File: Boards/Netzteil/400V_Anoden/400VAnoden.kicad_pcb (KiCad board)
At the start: 2 copper layers, 160 x 100 mm, 52 parts, among them P1 Drossel, P2 320V_AC, P3 Stabi, P4 133V_AC, P5 Stabi, P6 Trafo, P7 Trafo, P8 Relay, Q1 2SC2979

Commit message: Work in progess - many LAyour changes
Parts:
- added J1: Chassis_GND, MountingHole:MountingHole_3.2mm_M3_Pad_Via, F.Cu at (111.8, 111.8)
- moved REF** 9.03 mm to (111.8, 121.3)
- moved C2 4.70 mm to (59.1, 48.8)
- moved C8 4.70 mm to (59.1, 69.5)
- moved D2 3.81 mm to (69.2, 54.0)
- moved D4 3.81 mm to (67.3, 71.9)
- moved R1 3.81 mm to (79.4, 62.2)
- moved C15 1.91 mm to (65.4, 113.0)
- moved C16 1.91 mm to (65.4, 94.6)
- moved D7 1.91 mm to (75.6, 107.7)
- moved D8 1.91 mm to (85.7, 100.1)
- moved C12 1.52 mm to (84.1, 94.6)
- moved D10 1.52 mm to (56.1, 100.1)
- moved D9 1.52 mm to (66.3, 107.7)
- moved R8 1.52 mm to (70.9, 89.9)
- moved C11 1.52 mm to (84.0, 113.0)
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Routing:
- net Net-(C3-Pad1): track 99.6 -> 85.0 mm
- net Net-(C1-Pad1): track 49.3 -> 44.8 mm
- net Net-(C5-Pad1): track 227.6 -> 230.8 mm
- net Net-(C15-Pad2): track 26.4 -> 28.2 mm
- net Net-(C11-Pad1): track 31.6 -> 30.0 mm
- net /-180V_DC: track 167.4 -> 165.8 mm
- net Net-(C7-Pad2): track 74.1 -> 72.8 mm
- net Net-(D11-Pad2): track 26.6 -> 27.5 mm
- net Net-(D11-Pad1): track 31.0 -> 30.3 mm
- net GND: vias 46 -> 44
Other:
- rule pad_to_mask_clearance: 0.2 -> 0
- board text added: "Chassis GND"

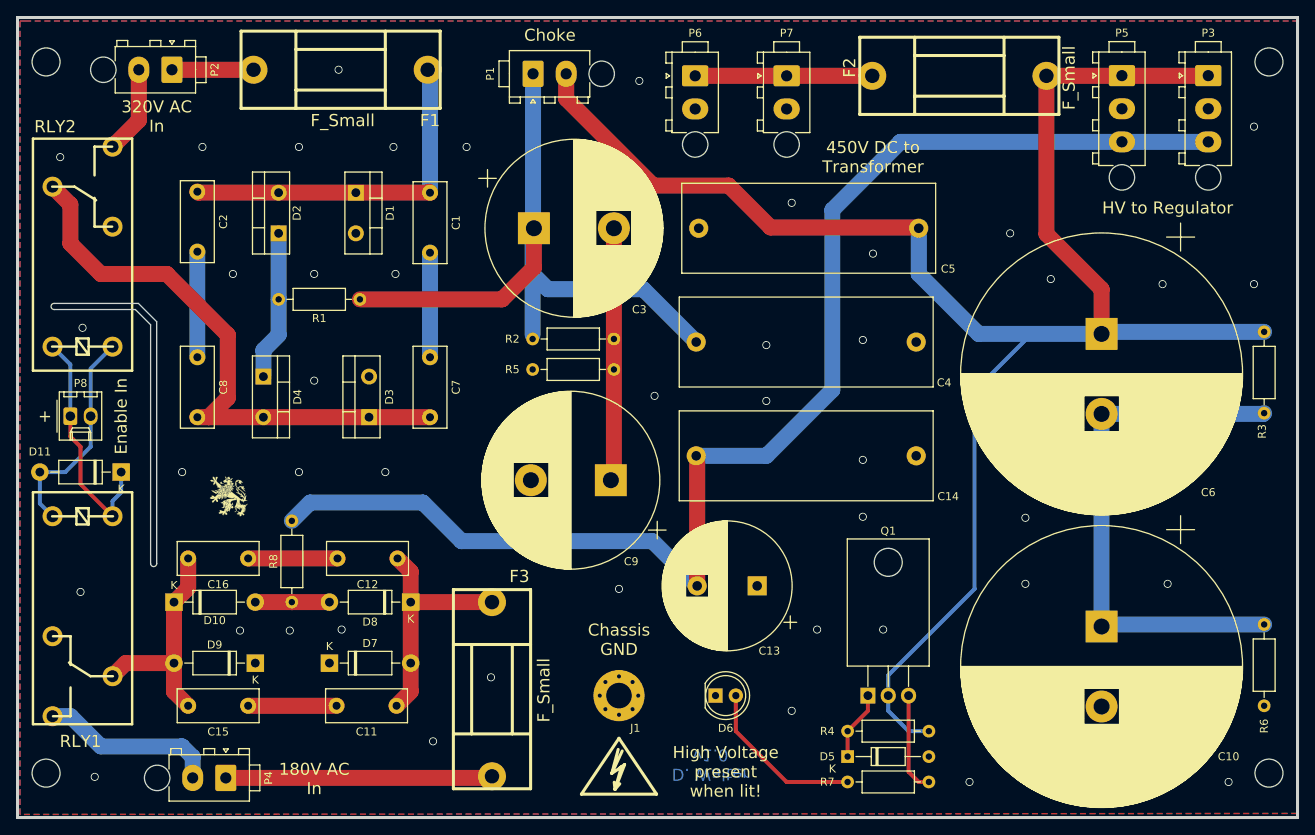
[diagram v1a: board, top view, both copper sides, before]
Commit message: 6.3V, 400V und 400V Regler Boards bestellt
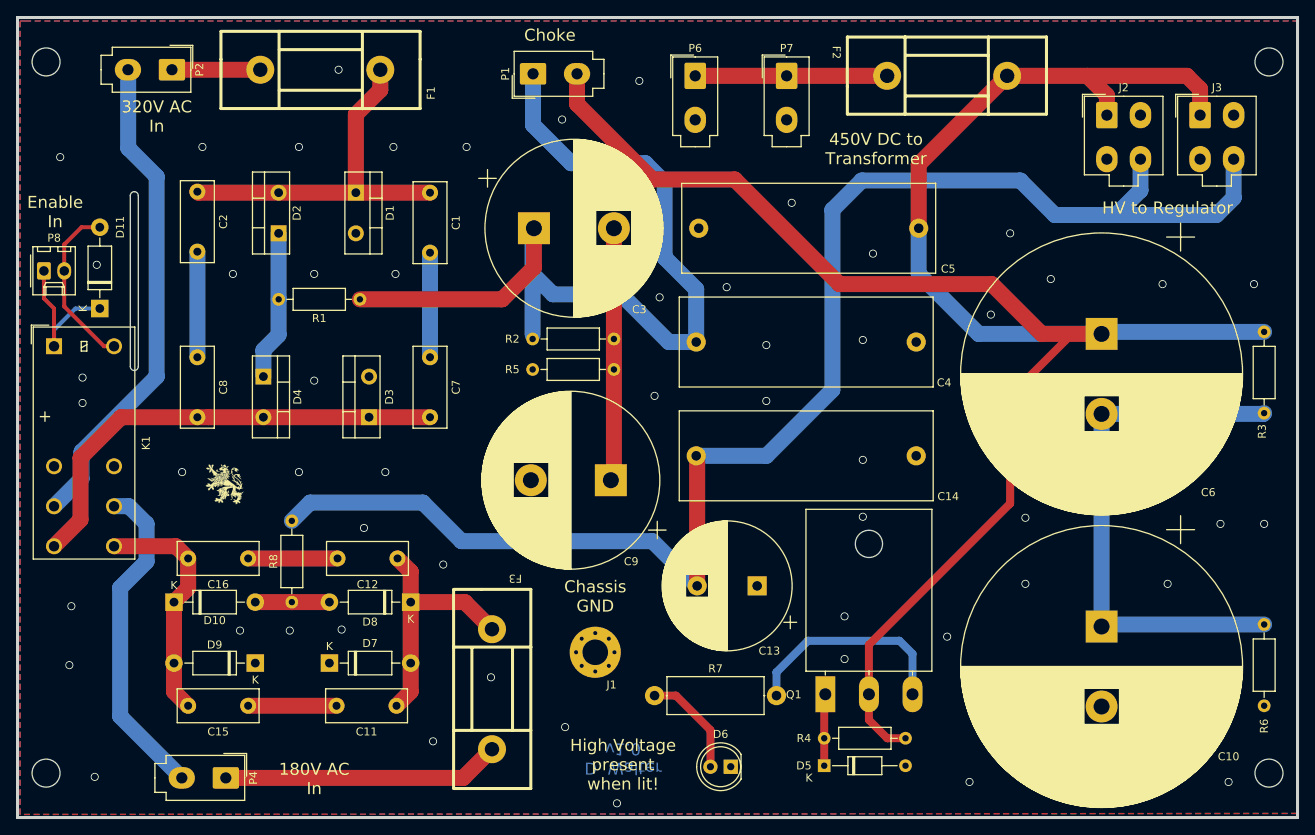
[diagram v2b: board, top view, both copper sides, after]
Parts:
- removed P3, P5: Stabi, Connector_TE-Connectivity:TE_MATE-N-LOK_1-770870-x_1x03_P4.14mm_Vertical
- removed the REF** at (111.8, 121.3)
- removed RLY1, RLY2: RELAY_40.51, w_relay:relay_40.51
- added J2: Conn_01x04, Connector_Molex:Molex_Mini-Fit_Jr_5566-04A_2x02_P4.20mm_Vertical, F.Cu at (172.7, 39.2)
- added J3: Conn_01x04, Connector_Molex:Molex_Mini-Fit_Jr_5566-04A_2x02_P4.20mm_Vertical, F.Cu at (184.4, 39.2)
- added K1: G2RL-2, Relay_THT:Relay_DPDT_Omron_G2RL-2, F.Cu at (41.1, 68.1)
- F1, F3: footprint w_misc_comp:fuse_holder_CQ-2 -> Fuse_Holder_Eska:Fuse__Holder_Eska_509100
- F2: value F_Small -> 500mAT; footprint w_misc_comp:fuse_holder_CQ-2 -> Fuse_Holder_Eska:Fuse__Holder_Eska_509100
- P1, P2, P4, P6, P7: footprint Connector_TE-Connectivity:TE_MATE-N-LOK_1-770866-x_1x02_P4.14mm_Vertical -> Connector_Molex:Molex_Mini-Fit_Jr_5566-02A_2x01_P4.20mm_Vertical
- Q1: value 2SC2979 -> S2000N; footprint Package_TO_SOT_THT:TO-220-3_Horizontal_TabDown -> Package_TO_SOT_THT:TO-3P-3_Horizontal_TabDown
- R7: footprint Resistor_THT:R_Axial_DIN0207_L6.3mm_D2.5mm_P10.16mm_Horizontal -> Resistor_THT:R_Axial_DIN0414_L11.9mm_D4.5mm_P15.24mm_Horizontal
- moved R7 26.4 mm to (116.2, 111.8)
- moved D11 20.6 mm to (46.9, 63.4), turned to 90 degrees
- moved P8 18.5 mm to (39.9, 58.7)
- moved D6 9.09 mm to (125.7, 120.7), turned to 180 degrees
- moved J1 6.17 mm to (108.8, 106.3)
- moved Q1 5.33 mm to (137.6, 111.6)
- moved D5 3.14 mm to (137.4, 120.5)
- moved R4 3.05 mm to (137.4, 117.1)
- moved F1 2.54 mm to (74.4, 33.5)
- moved G*** 1.61 mm to (62.5, 85.3)
- moved F2 1.52 mm to (152.8, 34.3)
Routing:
- net Net-(P2-P2): track 11.0 -> 61.3 mm
- net Net-(P1-P1): track 85.0 -> 112.9 mm
- net Net-(J2-Pin_1): track 230.8 -> 258.5 mm
- net Net-(P4-P2): track 22.2 -> 41.3 mm
- net /-180V_DC: track 165.8 -> 182.5 mm
- net Net-(Q1-E): track 12.0 -> 27.3 mm
- net Net-(D3-K): track 72.8 -> 58.2 mm
- net Net-(D11-K): track 30.3 -> 18.8 mm
- net Net-(D6-A): track 21.0 -> 13.3 mm
- net Net-(D11-A): track 27.5 -> 21.4 mm
- net /+450V_DC: track 22.1 -> 24.0 mm
- net Net-(D10-K): track 28.2 -> 29.8 mm
- net Net-(D7-A): track 30.0 -> 31.4 mm
- net Net-(P4-P1): track 33.6 -> 34.8 mm
- net Net-(D1-K): track 44.8 -> 45.8 mm
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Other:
- net class Default removed
